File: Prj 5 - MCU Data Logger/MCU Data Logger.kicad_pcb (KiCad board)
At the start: 4 copper layers, 51.4 x 45.7 mm, 30 parts, among them J1 Conn_01x04_Pin, J2 Conn_01x09_Pin, J3 Conn_01x04_Pin, J4 Conn_02x03_Odd_Even, U1 24LC1025, U2 DS1337S+, U3 24LC1025, U4 ATmega328P, Y1 32.768KHz, Y2 16MHz

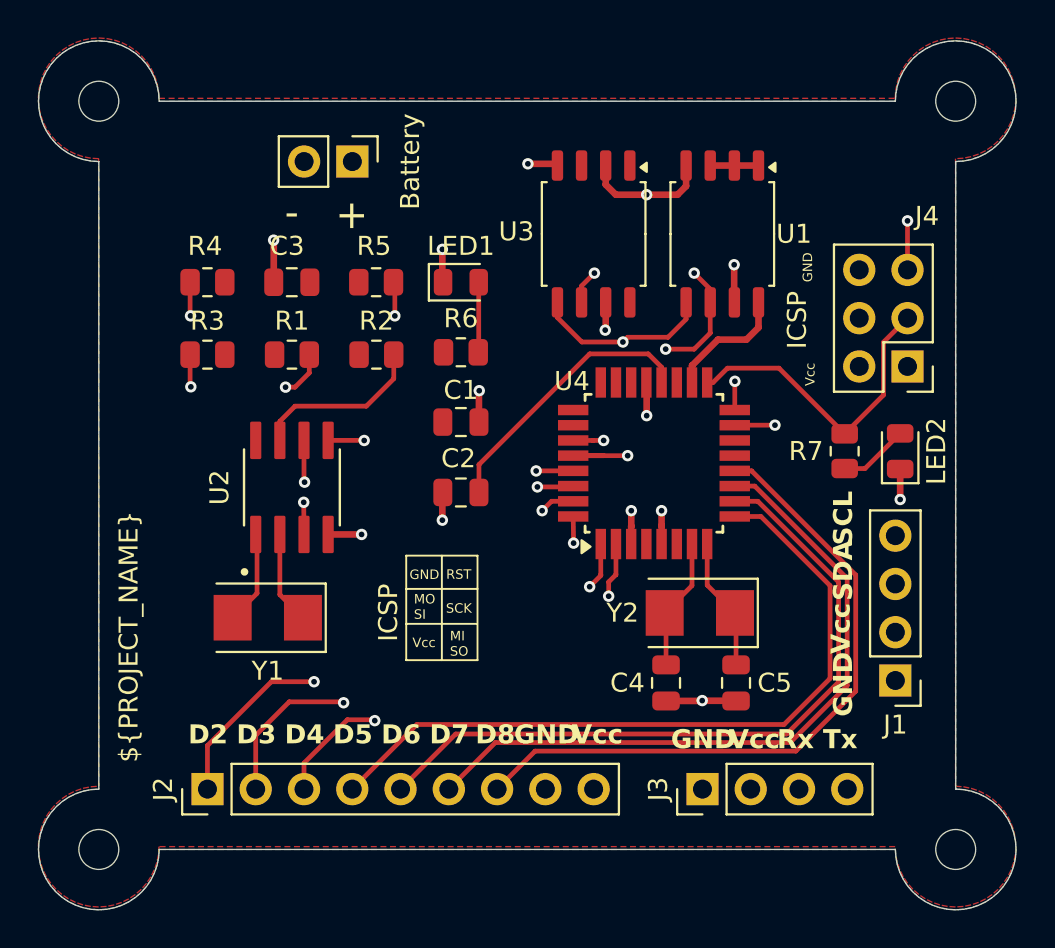
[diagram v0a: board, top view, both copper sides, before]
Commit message: Added net /AREF
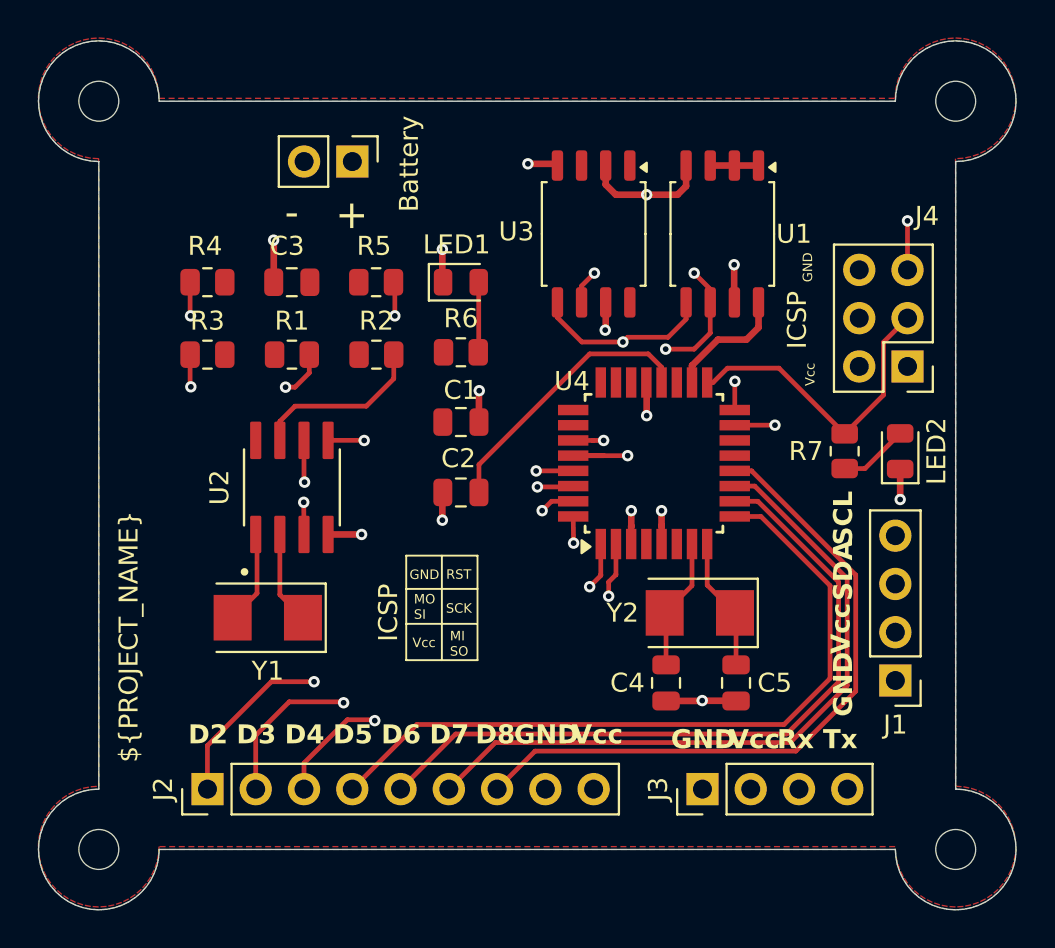
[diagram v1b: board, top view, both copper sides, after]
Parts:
- D1: value LED1 -> LED
- D2: value LED2 -> LED
- renumbered Battery to BT1
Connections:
- net Net-(U4-AREF) renamed /AREF
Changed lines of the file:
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@@
 	(net 1 "/BVcc")
 	(net 2 "GND")
-	(net 3 "Net-(U4-AREF)")
+	(net 3 "/AREF")
 	(net 4 "Net-(U4-XTAL1{slash}PB6)")
 	(net 5 "Net-(U4-XTAL2{slash}PB7)")
@@
 			(layers "F.Cu" "F.Paste" "F.Mask")
 			(roundrect_rratio 0.25)
-			(net 3 "Net-(U4-AREF)")
+			(net 3 "/AREF")
 			(pintype "passive")
 		)
@@
 			)
 		)
-		(property "Value" "LED2"
+		(property "Value" "LED"
 			(at 0 1.905 -90)
 			(layer "F.SilkS")
+			(hide yes)
 			(effects
 				(font
@@
 			)
 		)
+		(property "Value2" "LED2"
+			(at 0 1.911 90)
+			(unlocked yes)
+			(layer "F.SilkS")
+			(effects
+				(font
+					(size 1 1)
+					(thickness 0.15)
+				)
+			)
+		)
 		(property ki_fp_filters "LED* LED_SMD:* LED_THT:*")
 		(sheetname "Root")
@@
 			)
 		)
-		(property "Value" "LED1"
+		(property "Value" "LED"
 			(at 0 -1.905 0)
 			(layer "F.SilkS")
+			(hide yes)
 			(effects
 				(font
@@
 			)
 		)
+		(property "Value2" "LED1"
+			(at -0.225 -1.98 0)
+			(unlocked yes)
+			(layer "F.SilkS")
+			(effects
+				(font
+					(size 1 1)
+					(thickness 0.15)
+				)
+			)
+		)
 		(property ki_fp_filters "LED* LED_SMD:* LED_THT:*")
 		(sheetname "Root")
@@
 		(descr "Through hole straight pin header, 1x02, 2.54mm pitch, single row")
 		(tags "Through hole pin header THT 1x02 2.54mm single row")
-		(property "Reference" "Battery"
+		(property "Reference" "BT1"
 			(at 0 -3.043 90)
 			(layer "F.SilkS")
+			(hide yes)
 			(effects
 				(font
@@
 			(at 0 4.87 90)
 			(layer "F.Fab")
+			(hide yes)
 			(effects
 				(font
@@
 			)
 		)
+		(property "Value2" "Battery"
+			(at 0.12 -2.985 90)
+			(unlocked yes)
+			(layer "F.SilkS")
+			(effects
+				(font
+					(size 1 1)
+					(thickness 0.15)
+				)
+			)
+		)
 		(sheetname "Root")
 		(sheetfile "MCU Data Logger.kicad_sch")
@@
 			(size 1.6 0.55)
 			(layers "F.Cu" "F.Paste" "F.Mask")
-			(net 3 "Net-(U4-AREF)")
+			(net 3 "/AREF")
 			(pinfunction "AREF")
 			(pintype "passive")
